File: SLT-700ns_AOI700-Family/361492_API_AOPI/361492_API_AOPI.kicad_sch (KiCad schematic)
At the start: 11 parts, among them T1 CB, U1 12-Pin_SLx_Can

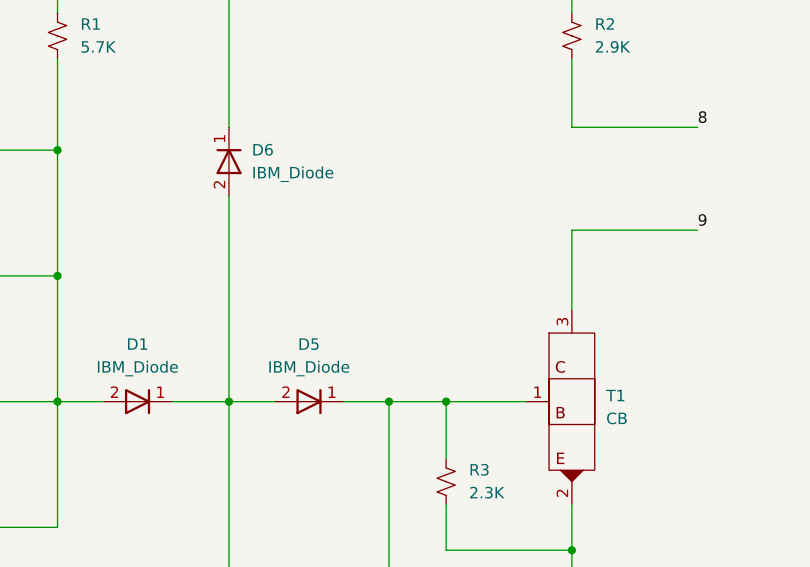
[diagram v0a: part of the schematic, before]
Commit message: Add can P/N to schematics for SLT-700
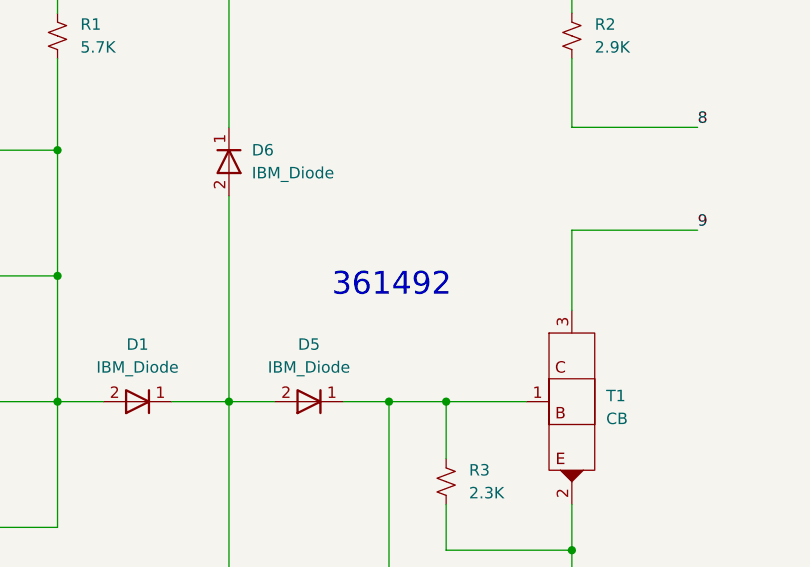
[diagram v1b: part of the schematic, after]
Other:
- note added: "361492"
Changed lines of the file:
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@@
     (effects (font (size 1.27 1.27)) (justify left bottom))
+  )
+  (text "361492" (at 129.54 82.55 0)
+    (effects (font (size 2.54 2.54)) (justify left bottom))
   )
   (label "8" (at 170.18 63.5 0)
